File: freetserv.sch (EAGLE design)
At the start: 62 parts, among them IC2 SN75240PW, Q1 12MHz, Q2 6MHz, U1 MCP16311-E/MS, U4 TLV810SDBZT, U5 SN74LVC1G86DCKR

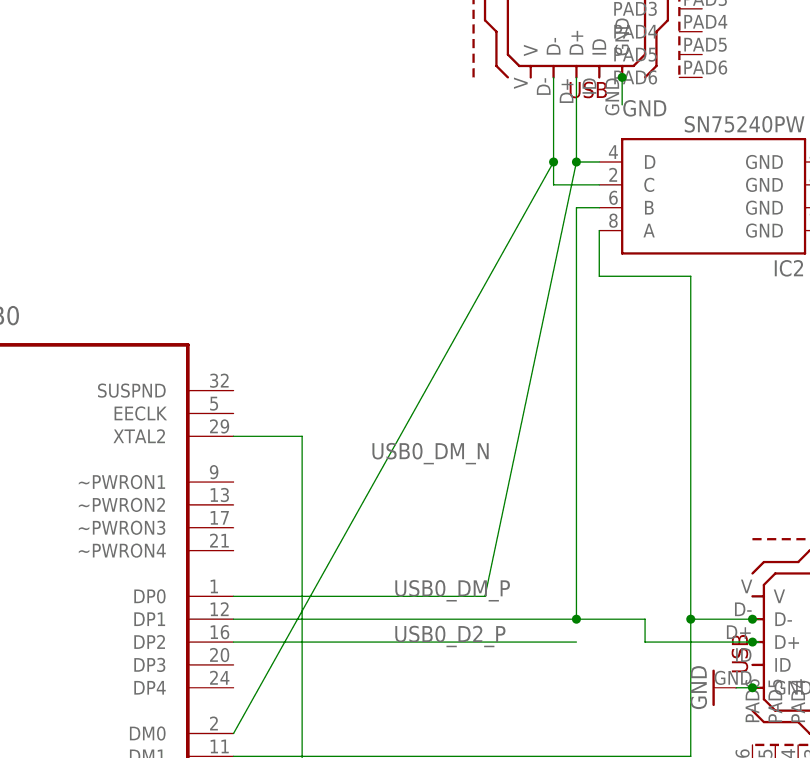
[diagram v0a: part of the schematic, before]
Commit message: Bugfix: add 1.5kΩ resistor to USB D+ to host
This is necessary for the host to recognize that a USB device was
plugged in. Without this resistor, nothing happens when you connect the
board to a computer.
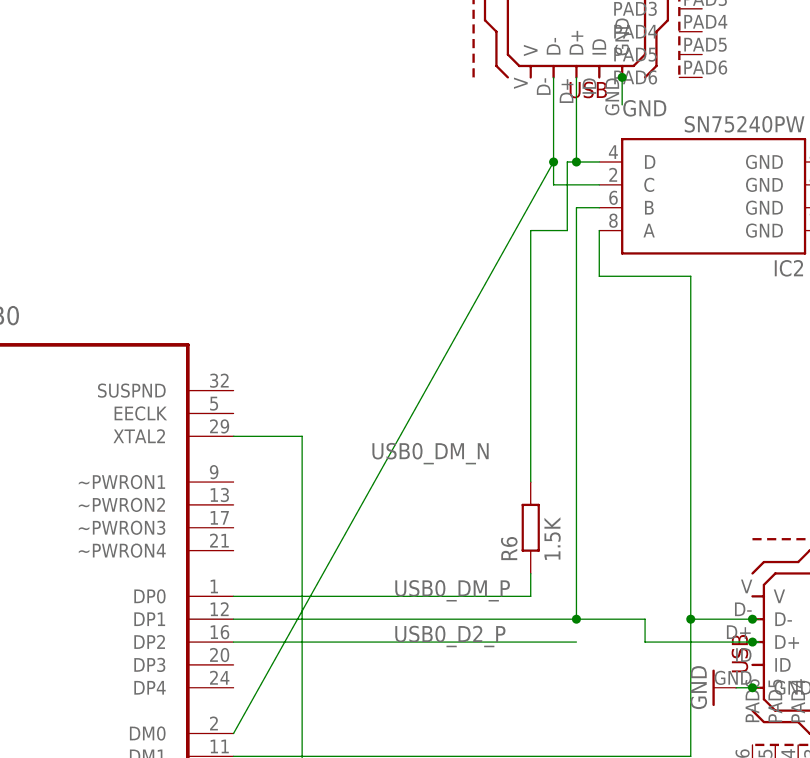
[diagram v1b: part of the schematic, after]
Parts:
- added R6: 1.5K, resistor:R-EU_R0805
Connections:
- new net N$41: IC2.D, R6.2, USB_RASPI_DATA.D+
- net USB0_DM_P: now also R6.1; no longer IC2.D, USB_RASPI_DATA.D+
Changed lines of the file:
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@@
 <?xml version="1.0" encoding="utf-8"?>
 <!DOCTYPE eagle SYSTEM "eagle.dtd">
-<eagle version="7.4.0">
+<eagle version="7.3.0">
 <drawing>
 <settings>
@@
 <part name="GND48" library="supply1" deviceset="GND" device=""/>
 <part name="GND49" library="supply1" deviceset="GND" device=""/>
+<part name="R6" library="resistor" deviceset="R-EU_" device="R0805" value="1.5K"/>
 </parts>
 <sheets>
@@
 <instance part="GND48" gate="1" x="119.38" y="246.38" rot="R90"/>
 <instance part="GND49" gate="1" x="119.38" y="243.84" rot="R90"/>
+<instance part="R6" gate="G$1" x="83.82" y="208.28" rot="R90"/>
 </instances>
 <busses>
@@
 <net name="USB0_DM_P" class="0">
 <segment>
-<pinref part="USB_RASPI_DATA" gate="G$1" pin="D+"/>
 <pinref part="HUB0" gate="A" pin="DP0"/>
-<wire x1="50.8" y1="200.66" x2="78.74" y2="200.66" width="0.1524" layer="91"/>
-<wire x1="78.74" y1="200.66" x2="88.9" y2="248.92" width="0.1524" layer="91"/>
+<wire x1="50.8" y1="200.66" x2="83.82" y2="200.66" width="0.1524" layer="91"/>
 <label x="68.58" y="200.66" size="1.778" layer="95"/>
-<pinref part="IC2" gate="G$1" pin="D"/>
-<wire x1="88.9" y1="248.92" x2="88.9" y2="258.318" width="0.1524" layer="91"/>
-<wire x1="88.9" y1="248.92" x2="91.44" y2="248.92" width="0.1524" layer="91"/>
-<junction x="88.9" y="248.92"/>
+<pinref part="R6" gate="G$1" pin="1"/>
+<wire x1="83.82" y1="200.66" x2="83.82" y2="203.2" width="0.1524" layer="91"/>
 </segment>
 </net>
@@
 </segment>
 </net>
+<net name="N$41" class="0">
+<segment>
+<pinref part="IC2" gate="G$1" pin="D"/>
+<wire x1="88.9" y1="248.92" x2="91.44" y2="248.92" width="0.1524" layer="91"/>
+<pinref part="USB_RASPI_DATA" gate="G$1" pin="D+"/>
+<wire x1="88.9" y1="248.92" x2="88.9" y2="258.318" width="0.1524" layer="91"/>
+<pinref part="R6" gate="G$1" pin="2"/>
+<wire x1="83.82" y1="213.36" x2="83.82" y2="241.3" width="0.1524" layer="91"/>
+<wire x1="83.82" y1="241.3" x2="87.884" y2="241.3" width="0.1524" layer="91"/>
+<wire x1="88.9" y1="248.92" x2="87.884" y2="248.92" width="0.1524" layer="91"/>
+<wire x1="87.884" y1="248.92" x2="87.884" y2="241.3" width="0.1524" layer="91"/>
+<junction x="88.9" y="248.92"/>
+</segment>
+</net>

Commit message: Replace all 100nF capacitors with 0.1uF (which is the same)
Since capacitors are labelled as 0.1uF, this makes it more clear which
part goes where.

fixes #8
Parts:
- C11, C12, C4: value 100nF -> 0.1uF
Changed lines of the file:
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@@
 <part name="FERRITE1" library="Wurth_Elektronik_Passive_rev15d" deviceset="WE-KI" device="_0805A" value="330"/>
 <part name="FERRITE2" library="Wurth_Elektronik_Passive_rev15d" deviceset="WE-KI" device="_0805A" value="330"/>
-<part name="C11" library="resistor" deviceset="C-EU" device="C0805" value="100nF"/>
-<part name="C12" library="resistor" deviceset="C-EU" device="C0805" value="100nF"/>
+<part name="C11" library="resistor" deviceset="C-EU" device="C0805" value="0.1uF"/>
+<part name="C12" library="resistor" deviceset="C-EU" device="C0805" value="0.1uF"/>
 <part name="C13" library="resistor" deviceset="C-EU" device="C0805" value="4.7uF"/>
 <part name="C14" library="resistor" deviceset="C-EU" device="C0805" value="4.7uF"/>
@@
 <part name="U$1" library="stewart_ss73100_046f_dwg" deviceset="SS73100-046F_DWG" device=""/>
 <part name="U1" library="microchip" deviceset="MCP16311" device="-E/MS"/>
-<part name="C4" library="resistor" deviceset="C-EU" device="C0805" value="100nF"/>
+<part name="C4" library="resistor" deviceset="C-EU" device="C0805" value="0.1uF"/>
 <part name="L3" library="inductor-taiyoyuden" deviceset="NR6028" device="T220M" value="15uH"/>
 <part name="R4" library="resistor" deviceset="R-EU_" device="R0805" value="31.6k"/>

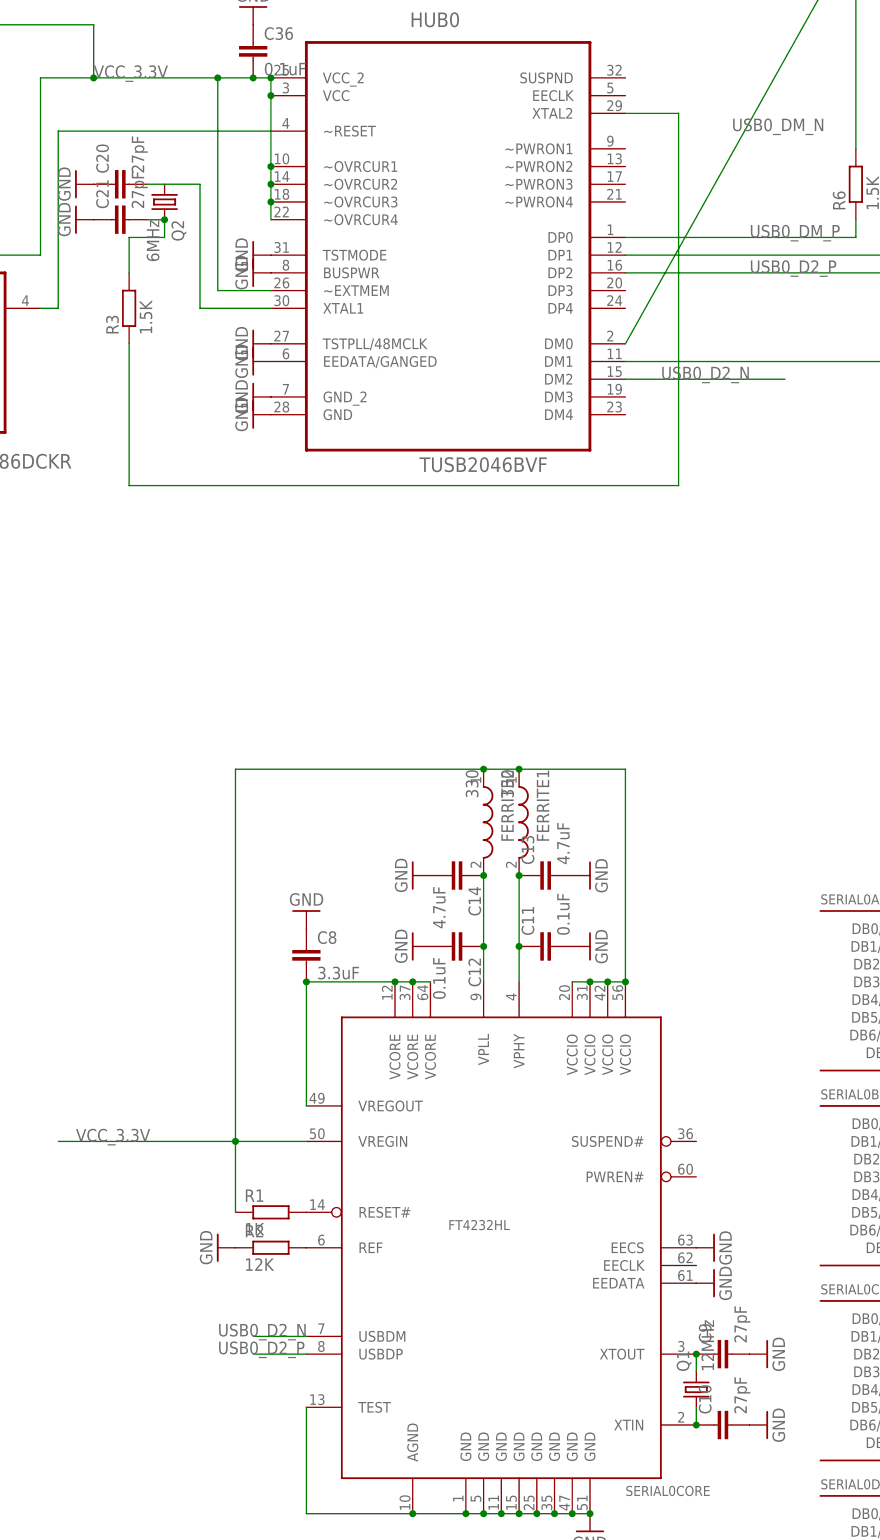
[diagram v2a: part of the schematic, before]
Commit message: use 18pF capacitors to match the crystals
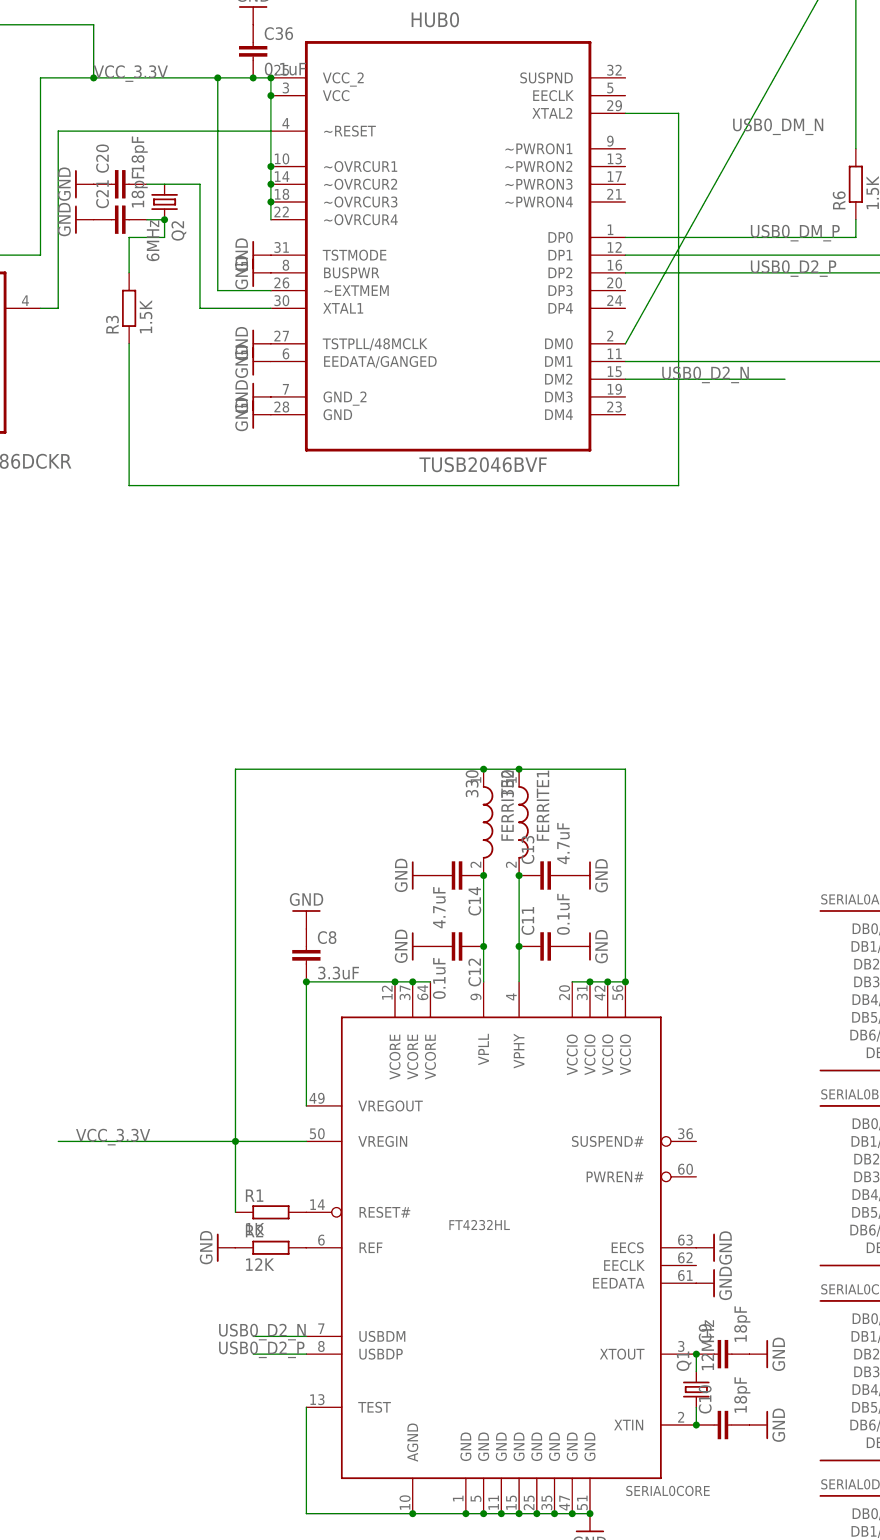
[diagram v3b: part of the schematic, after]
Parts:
- C10, C20, C21, C9: value 27pF -> 18pF
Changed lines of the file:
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@@
 <part name="GND16" library="supply1" deviceset="GND" device=""/>
 <part name="Q1" library="crystal" deviceset="CSM-7X-DU" device="" value="12MHz"/>
-<part name="C9" library="resistor" deviceset="C-EU" device="C0805" value="27pF"/>
-<part name="C10" library="resistor" deviceset="C-EU" device="C0805" value="27pF"/>
+<part name="C9" library="resistor" deviceset="C-EU" device="C0805" value="18pF"/>
+<part name="C10" library="resistor" deviceset="C-EU" device="C0805" value="18pF"/>
 <part name="GND17" library="supply1" deviceset="GND" device=""/>
 <part name="GND18" library="supply1" deviceset="GND" device=""/>
@@
 <part name="GND32" library="supply1" deviceset="GND" device=""/>
 <part name="Q2" library="crystal" deviceset="CSM-7X-DU" device="" value="6MHz"/>
-<part name="C20" library="resistor" deviceset="C-EU" device="C0805" value="27pF"/>
-<part name="C21" library="resistor" deviceset="C-EU" device="C0805" value="27pF"/>
+<part name="C20" library="resistor" deviceset="C-EU" device="C0805" value="18pF"/>
+<part name="C21" library="resistor" deviceset="C-EU" device="C0805" value="18pF"/>
 <part name="GND34" library="supply1" deviceset="GND" device=""/>
 <part name="GND35" library="supply1" deviceset="GND" device=""/>

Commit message: assign part numbers for almost all parts
The remaining parts are possibly subject to change.

This was done using the bom-ex ULP:
http://www.cadsoftusa.com/downloads/file/bom-ex164.zip

fixes #10
fixes #13
fixes #14
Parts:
- C1, C11, C12, C15, C16, C17, C18, C19, C22, C23, C24, C25, C26, C27, C28, C29, C30, C31, C32, C33, C34, C35, C36, C4: PARTNO (none) -> 1276-1003-1-ND
- C10, C20, C21, C9: PARTNO (none) -> 709-1171-1-ND
- C13, C14: PARTNO (none) -> 587-1302-1-ND
- C2, C3, C6, C7: PARTNO (none) -> 311-1459-1-ND
- C5: PARTNO (none) -> 311-1365-1-ND
- C8: PARTNO (none) -> 445-7589-1-ND
- DRIVER0A, DRIVER0B, DRIVER0B1, DRIVER0B2: PARTNO (none) -> 296-19263-1-ND
- FERRITE1, FERRITE2: PARTNO (none) -> 490-5988-1-ND
- HUB0: PARTNO (none) -> 296-27131-1-ND
- L3: PARTNO (none) -> 587-2624-1-ND
- Q1: PARTNO (none) -> 535-10218-1-ND
- Q2: PARTNO (none) -> 535-10208-1-ND
- R1: PARTNO (none) -> 311-1.0KARCT-ND
- R2: PARTNO (none) -> 311-12.0KCRCT-ND
- R3, R6: PARTNO (none) -> 311-1.5KARCT-ND
- R4: PARTNO (none) -> 311-31.6KCRCT-ND
- R5: PARTNO (none) -> 311-10KARCT-ND
- SERIAL0: PARTNO (none) -> 768-1026-1-ND
- U$1: PARTNO (none) -> 380-1225-ND
- U1: PARTNO (none) -> MCP16311-E/MS-ND

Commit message: rename VCC/VCC_3.3V to +5V and +3V3, use appropriate supply pins
Also disconnect the power supply part from the USB hub so that we have
an easier time adding the R/C circuit.
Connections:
- net VCC renamed +5V
- net VCC_3.3V renamed +3V3
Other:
- moved on the sheet: C2, C3, C36, C4, C5, C6, C7, L3, R4, R5, U1
